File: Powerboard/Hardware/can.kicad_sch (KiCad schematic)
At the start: 11 parts, among them U5 SN65HVD230

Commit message: waiting for review
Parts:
- removed JP1: TermJP, Jumper:SolderJumper-3_P1.3mm_Open_RoundedPad1.0x1.5mm, symbol Jumper:SolderJumper_2_Open
- added R23: 0, Resistor_SMD:R_0402_1005Metric, symbol Device:R
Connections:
- net Vref: now also R23.1
- net at C20.1, R16.2, R17.1: now also R23.2
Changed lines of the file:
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@@
     (pin "8")
+  )
+  (symbol (lib_id "Device:R") (at 140.97 92.456 90) (unit 1)
+    (in_bom yes) (on_board yes) (fields_autoplaced)
+    (property "Reference" "R23" (id 0) (at 140.97 87.7402 90))
+    (property "Value" "0" (id 1) (at 140.97 90.2771 90))
+    (property "Footprint" "Resistor_SMD:R_0402_1005Metric" (id 2) (at 140.97 94.234 90)
+      (effects (font (size 1.27 1.27)) hide)
+    )
+    (property "Datasheet" "~" (id 3) (at 140.97 92.456 0)
+      (effects (font (size 1.27 1.27)) hide)
+    )
+    (pin "1")
+    (pin "2")
   )
   (symbol (lib_id "power:GND") (at 158.75 92.456 0) (unit 1)
@@
     (pin "1")
   )
-  (symbol (lib_id "Jumper:SolderJumper_2_Open") (at 140.97 92.456 0) (unit 1)
-    (in_bom yes) (on_board yes) (fields_autoplaced)
-    (property "Reference" "JP1" (id 0) (at 140.97 86.106 0))
-    (property "Value" "TermJP" (id 1) (at 140.97 88.646 0))
-    (property "Footprint" "Jumper:SolderJumper-3_P1.3mm_Open_RoundedPad1.0x1.5mm" (id 2) (at 140.97 92.456 0)
-      (effects (font (size 1.27 1.27)) hide)
-    )
-    (property "Datasheet" "~" (id 3) (at 140.97 92.456 0)
-      (effects (font (size 1.27 1.27)) hide)
-    )
-    (pin "1")
-    (pin "2")
-  )
   (symbol (lib_id "power:GND") (at 158.75 106.426 0) (unit 1)

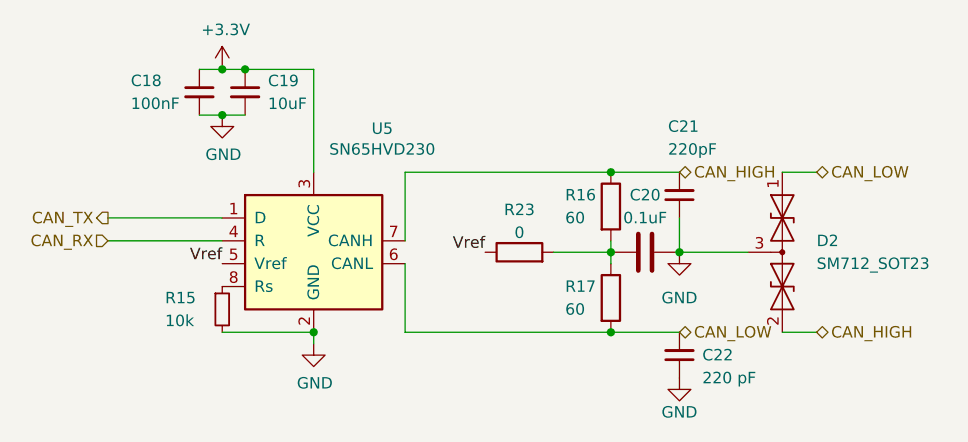
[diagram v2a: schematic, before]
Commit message: vias fixed, ready for review
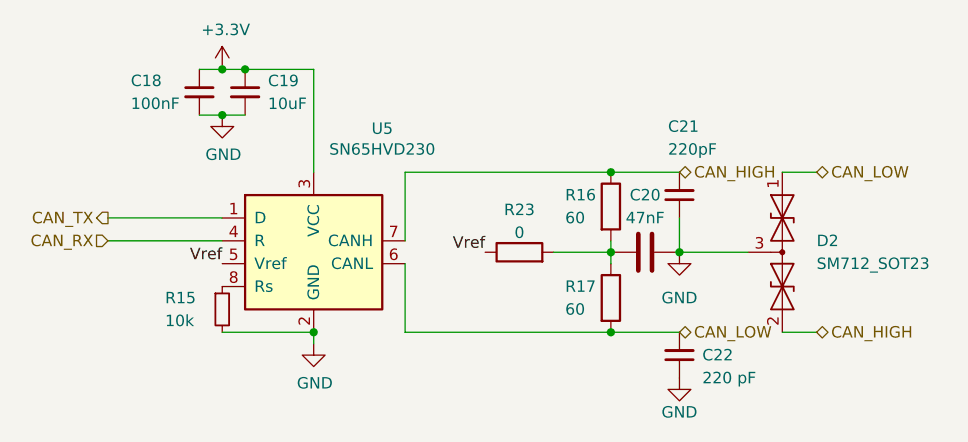
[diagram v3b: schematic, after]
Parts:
- C20: value 0.1uF -> 47nF
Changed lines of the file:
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@@
       (effects (font (size 1.27 1.27)))
     )
-    (property "Value" "0.1uF" (at 154.94 88.646 90)
+    (property "Value" "47nF" (at 154.94 88.646 90)
       (effects (font (size 1.27 1.27)))
     )

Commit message: reviewed
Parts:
- removed C21: 220pF, Capacitor_SMD:C_0402_1005Metric, symbol Device:C_Small
- removed C22: 220 pF, Capacitor_SMD:C_0402_1005Metric, symbol Device:C_Small
- R15: value 10k -> 0; footprint Resistor_SMD:R_0402_1005Metric -> Resistor_SMD:R_0603_1608Metric
- R16, R17: footprint Resistor_SMD:R_0402_1005Metric -> Resistor_SMD:R_0603_1608Metric
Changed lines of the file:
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@@
-    (stroke (width 0) (type default))
-  )
-  (wire (pts (xy 158.75 88.646) (xy 158.75 92.456))
     (stroke (width 0) (type default))
   )
@@
         (path "/e63e39d7-6ac0-4ffd-8aa3-1841a4541b55/12646a0c-a158-4f1c-9172-cd278d717c5e"
           (reference "D2") (unit 1)
-        )
-      )
-    )
-  )
-  (symbol (lib_id "Device:C_Small") (at 158.75 103.886 180) (unit 1)
-    (in_bom yes) (on_board yes) (dnp no) (fields_autoplaced)
-    (property "Reference" "C22" (at 161.29 103.886 0)
-      (effects (font (size 1.27 1.27)) (justify right))
-    )
-    (property "Value" "220 pF" (at 161.29 106.426 0)
-      (effects (font (size 1.27 1.27)) (justify right))
-    )
-    (property "Footprint" "Capacitor_SMD:C_0402_1005Metric" (at 158.75 103.886 0)
-      (effects (font (size 1.27 1.27)) hide)
-    )
-    (property "Datasheet" "~" (at 158.75 103.886 0)
-      (effects (font (size 1.27 1.27)) hide)
-    )
-    (pin "1")
-    (pin "2")
-    (instances
-      (project "Switcher"
-        (path "/e63e39d7-6ac0-4ffd-8aa3-1841a4541b55/12646a0c-a158-4f1c-9172-cd278d717c5e"
-          (reference "C22") (unit 1)
         )
       )
@@
       (effects (font (size 1.27 1.27)) (justify left))
     )
-    (property "Value" "10k" (at 101.6 100.076 0)
-      (effects (font (size 1.27 1.27)) (justify left))
-    )
-    (property "Footprint" "Resistor_SMD:R_0402_1005Metric" (at 107.95 98.806 0)
+    (property "Value" "0" (at 101.6 100.076 0)
+      (effects (font (size 1.27 1.27)) (justify left))
+    )
+    (property "Footprint" "Resistor_SMD:R_0603_1608Metric" (at 107.95 98.806 0)
       (effects (font (size 1.27 1.27)) hide)
     )
@@
       (effects (font (size 1.27 1.27)) (justify left))
     )
-    (property "Footprint" "Resistor_SMD:R_0402_1005Metric" (at 149.352 97.536 90)
+    (property "Footprint" "Resistor_SMD:R_0603_1608Metric" (at 149.352 97.536 90)
       (effects (font (size 1.27 1.27)) hide)
     )
@@
     )
   )
-  (symbol (lib_id "Device:C_Small") (at 158.75 86.106 180) (unit 1)
-    (in_bom yes) (on_board yes) (dnp no)
-    (property "Reference" "C21" (at 157.48 78.486 0)
-      (effects (font (size 1.27 1.27)) (justify right))
-    )
-    (property "Value" "220pF" (at 157.48 81.026 0)
-      (effects (font (size 1.27 1.27)) (justify right))
-    )
-    (property "Footprint" "Capacitor_SMD:C_0402_1005Metric" (at 158.75 86.106 0)
-      (effects (font (size 1.27 1.27)) hide)
-    )
-    (property "Datasheet" "~" (at 158.75 86.106 0)
-      (effects (font (size 1.27 1.27)) hide)
-    )
-    (pin "1")
-    (pin "2")
-    (instances
-      (project "Switcher"
-        (path "/e63e39d7-6ac0-4ffd-8aa3-1841a4541b55/12646a0c-a158-4f1c-9172-cd278d717c5e"
-          (reference "C21") (unit 1)
-        )
-      )
-    )
-  )
   (symbol (lib_id "Device:R") (at 151.13 87.376 0) (unit 1)
     (in_bom yes) (on_board yes) (dnp no) (fields_autoplaced)
@@
       (effects (font (size 1.27 1.27)) (justify left))
     )
-    (property "Footprint" "Resistor_SMD:R_0402_1005Metric" (at 149.352 87.376 90)
+    (property "Footprint" "Resistor_SMD:R_0603_1608Metric" (at 149.352 87.376 90)
       (effects (font (size 1.27 1.27)) hide)
     )
@@
         )
       )
-    )
-  )
-  (symbol (lib_id "power:GND") (at 158.75 106.426 0) (unit 1)
-    (in_bom yes) (on_board yes) (dnp no) (fields_autoplaced)
-    (property "Reference" "#PWR0139" (at 158.75 112.776 0)
-      (effects (font (size 1.27 1.27)) hide)
-    )
-    (property "Value" "GND" (at 158.75 110.236 0)
-      (effects (font (size 1.27 1.27)))
-    )
-    (property "Footprint" "" (at 158.75 106.426 0)
-      (effects (font (size 1.27 1.27)) hide)
-    )
-    (property "Datasheet" "" (at 158.75 106.426 0)
-      (effects (font (size 1.27 1.27)) hide)
-    )
-    (pin "1")
-    (instances
-      (project "Switcher"
-        (path "/e63e39d7-6ac0-4ffd-8aa3-1841a4541b55/12646a0c-a158-4f1c-9172-cd278d717c5e"
-          (reference "#PWR0139") (unit 1)
-        )
-      )

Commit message: changes
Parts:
- C19: footprint Capacitor_SMD:C_0603_1608Metric -> Capacitor_SMD:C_0402_1005Metric
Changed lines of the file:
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@@
       (effects (font (size 1.27 1.27)) (justify left))
     )
-    (property "Footprint" "Capacitor_SMD:C_0603_1608Metric" (at 110.49 74.676 0)
+    (property "Footprint" "Capacitor_SMD:C_0402_1005Metric" (at 110.49 74.676 0)
       (effects (font (size 1.27 1.27)) hide)
     )
